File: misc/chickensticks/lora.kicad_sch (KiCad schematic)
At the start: 30 parts, among them J8 S02-25200300, J9 SMA, U4 LR2021IMLTRT, Y2 TG2520SMN 32.0000M-MCGNNM0

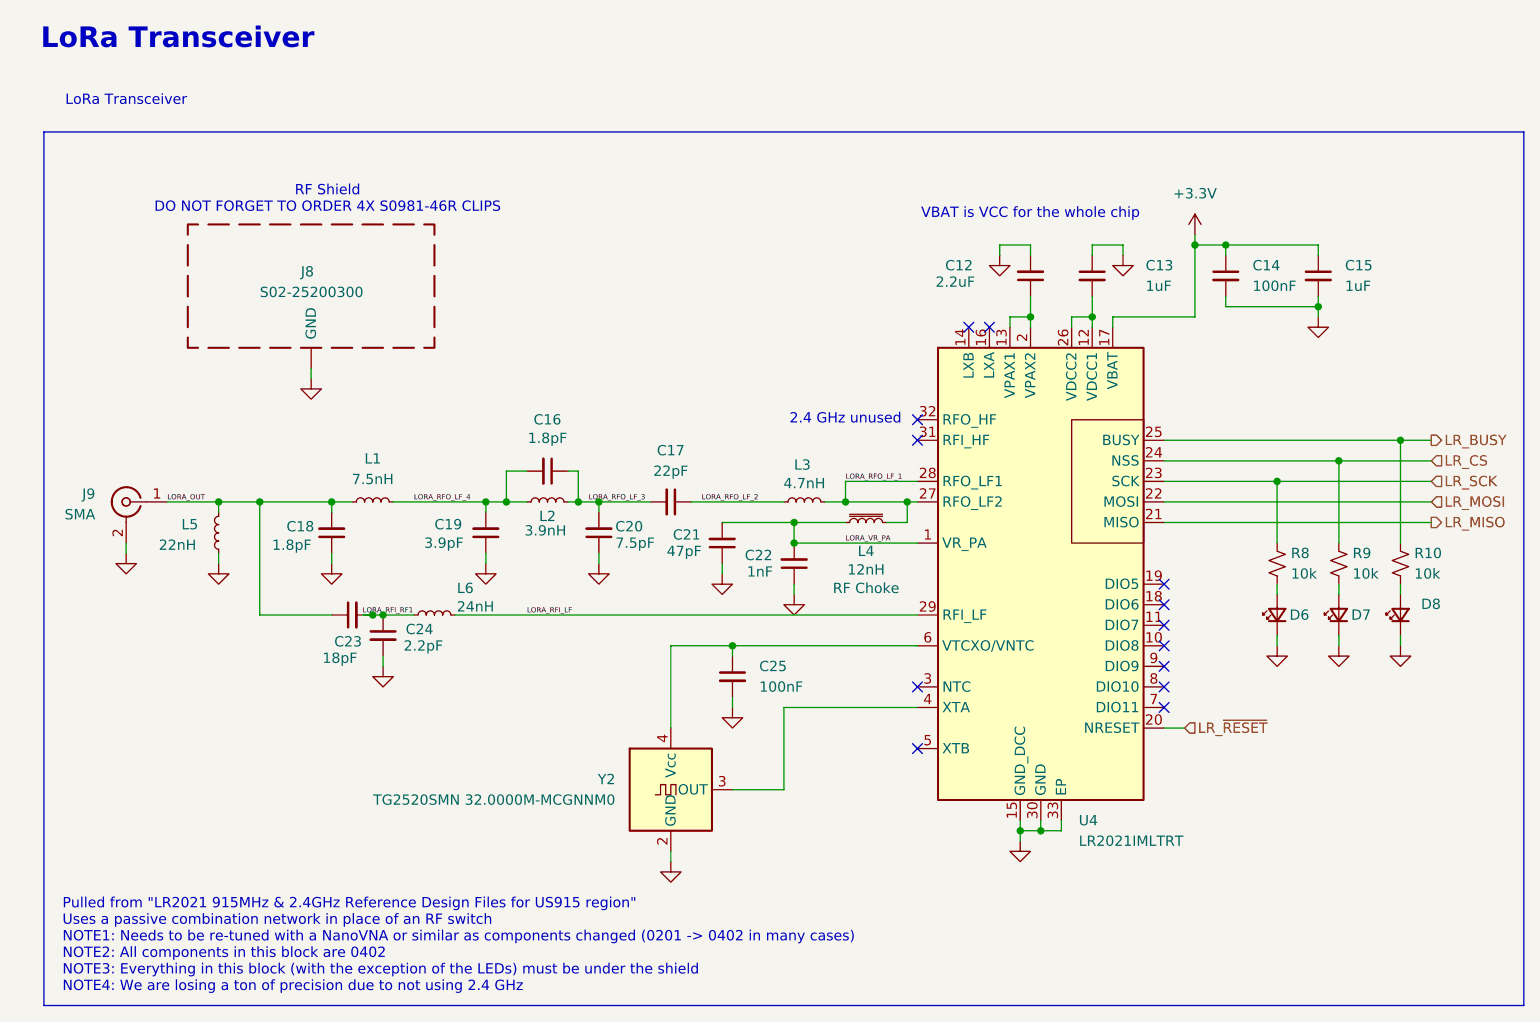
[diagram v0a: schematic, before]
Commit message: the great flatpak and kicad 10.0.6 migration
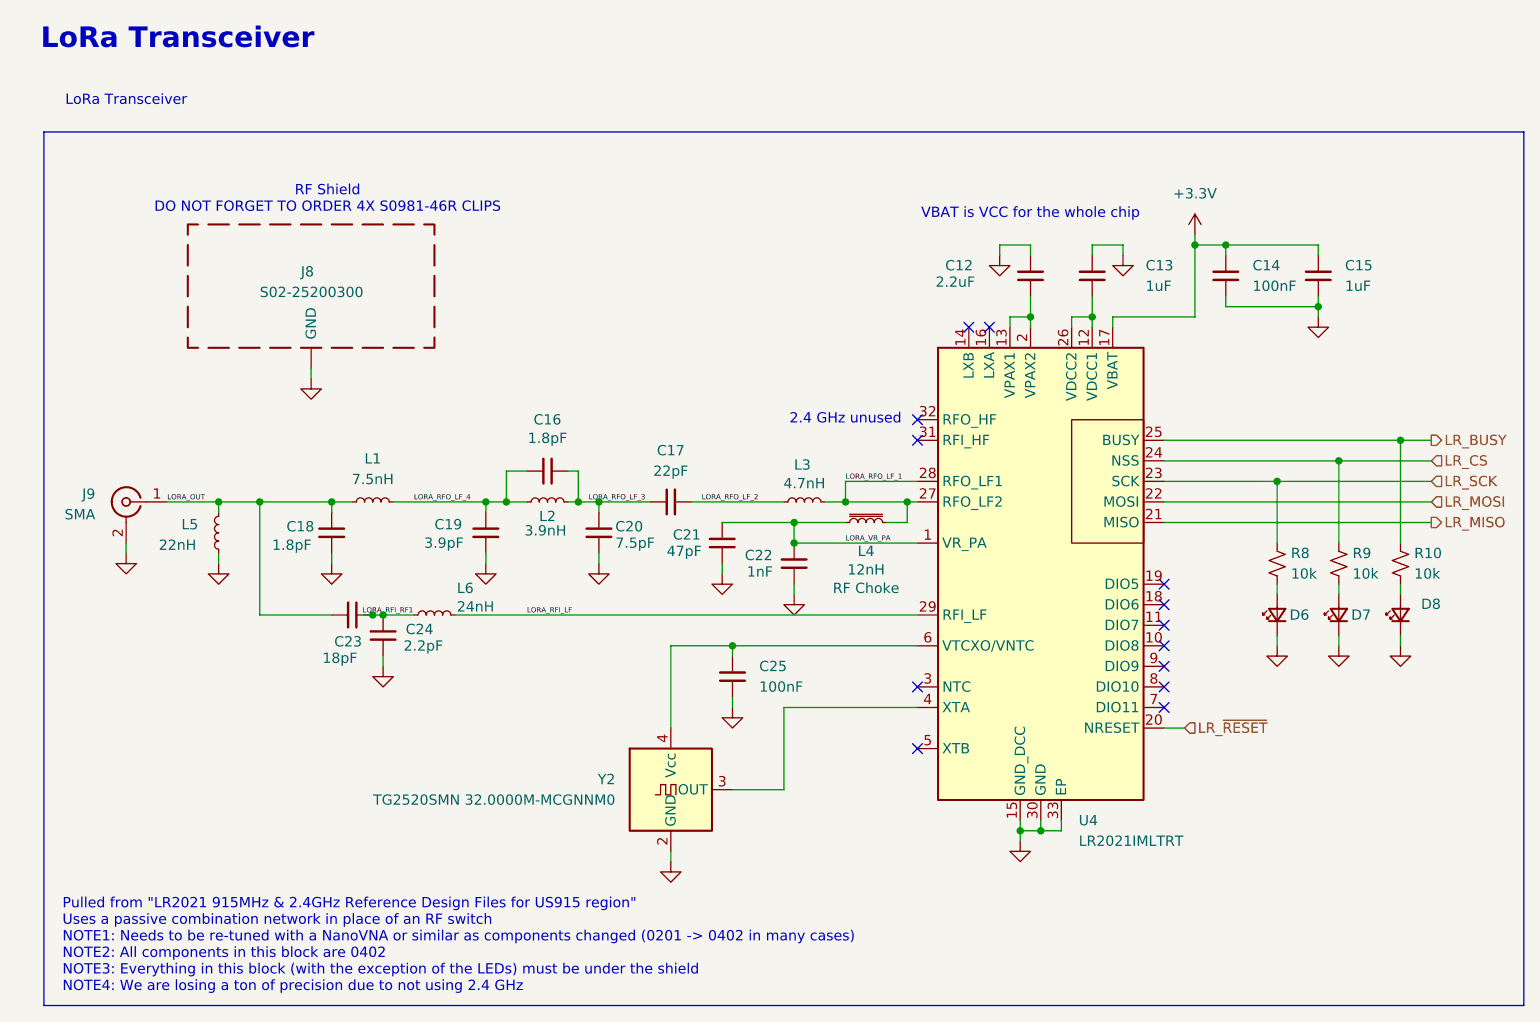
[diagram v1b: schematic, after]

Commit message: Document setup, update template, and use an ampersand when referring to APRL
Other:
- company: Aggie Propulsion and Rocketry Lab -> Aggie Propulsion & Rocketry Lab
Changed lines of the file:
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@@
 		(title "Chickenstick")
 		(rev "0")
-		(company "Aggie Propulsion and Rocketry Lab")
+		(company "Aggie Propulsion & Rocketry Lab")
 		(comment 1 "Drawn by: Nolan Poe")
 		(comment 2 "Reviewed by: Daniel Fan (and hopefully Tim Solberg)")
